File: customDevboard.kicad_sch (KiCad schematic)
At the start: 78 parts, among them J1 USB_C_Receptacle_USB2.0_14P, J10 GPIO29_ADC3, J11 GND, J12 GPIO0, J13 GPIO1, J14 GPIO2, J15 GPIO3, J16 GPIO4, J17 GPIO5, J18 GPIO6, J19 GPIO7, J2 RUN, J20 GPIO8, J21 GPIO9, J22 Conn_01x01, J23 Conn_01x01, J24 Conn_01x01, J25 Conn_01x01, J26 Conn_01x01, J27 Conn_01x01, J28 Conn_01x01, J29 Conn_01x01, J3 3V3, J30 Conn_01x01, J31 Conn_01x01, J32 Conn_01x01, J33 Conn_01x01, J34 Conn_01x01, J35 Conn_01x01, J36 Conn_01x01, J37 Conn_01x01, J38 Conn_01x01, J39 Conn_01x01, J4 VBUS, J40 Conn_01x01, J41 Conn_01x01, J42 SWCLK, J43 GND, J44 SWD, J5 GND, J6 GND, J7 GPIO26_ADC0, J8 GPIO27_ADC1, J9 GPIO28_ADC2, SW1 BOOT, U1 RP2040, U2 W25Q128JVP, U3 TLV75733PDRV, Y1 12 MHz

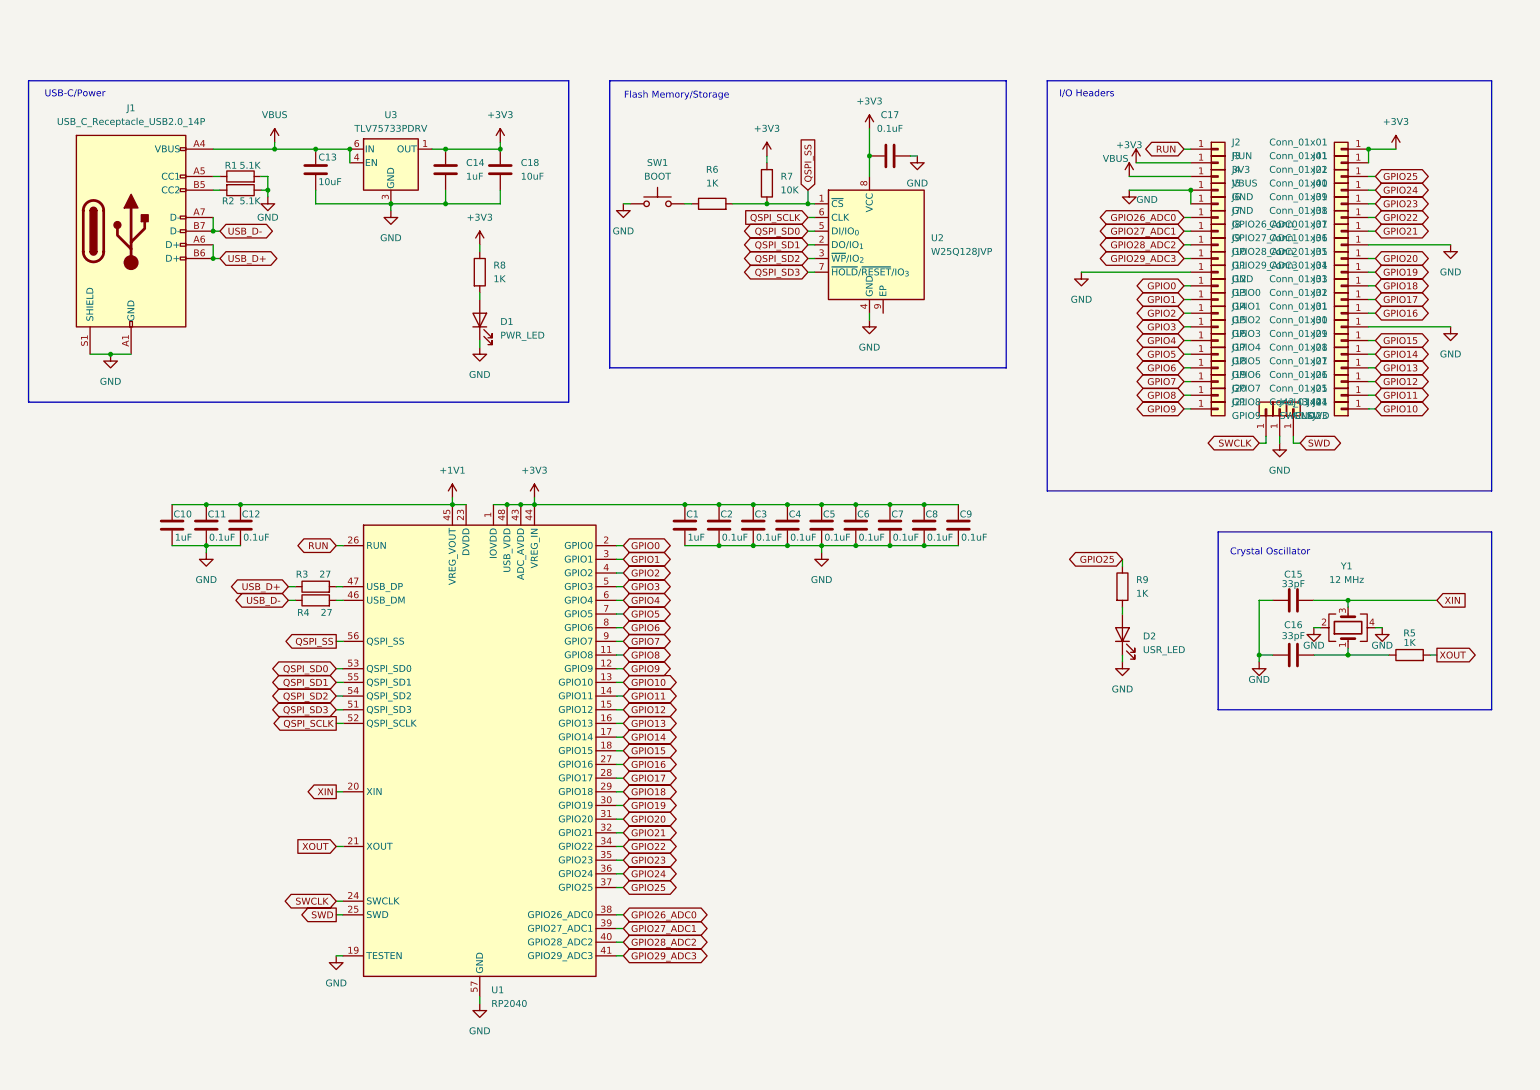
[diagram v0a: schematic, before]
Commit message: switch to stm32
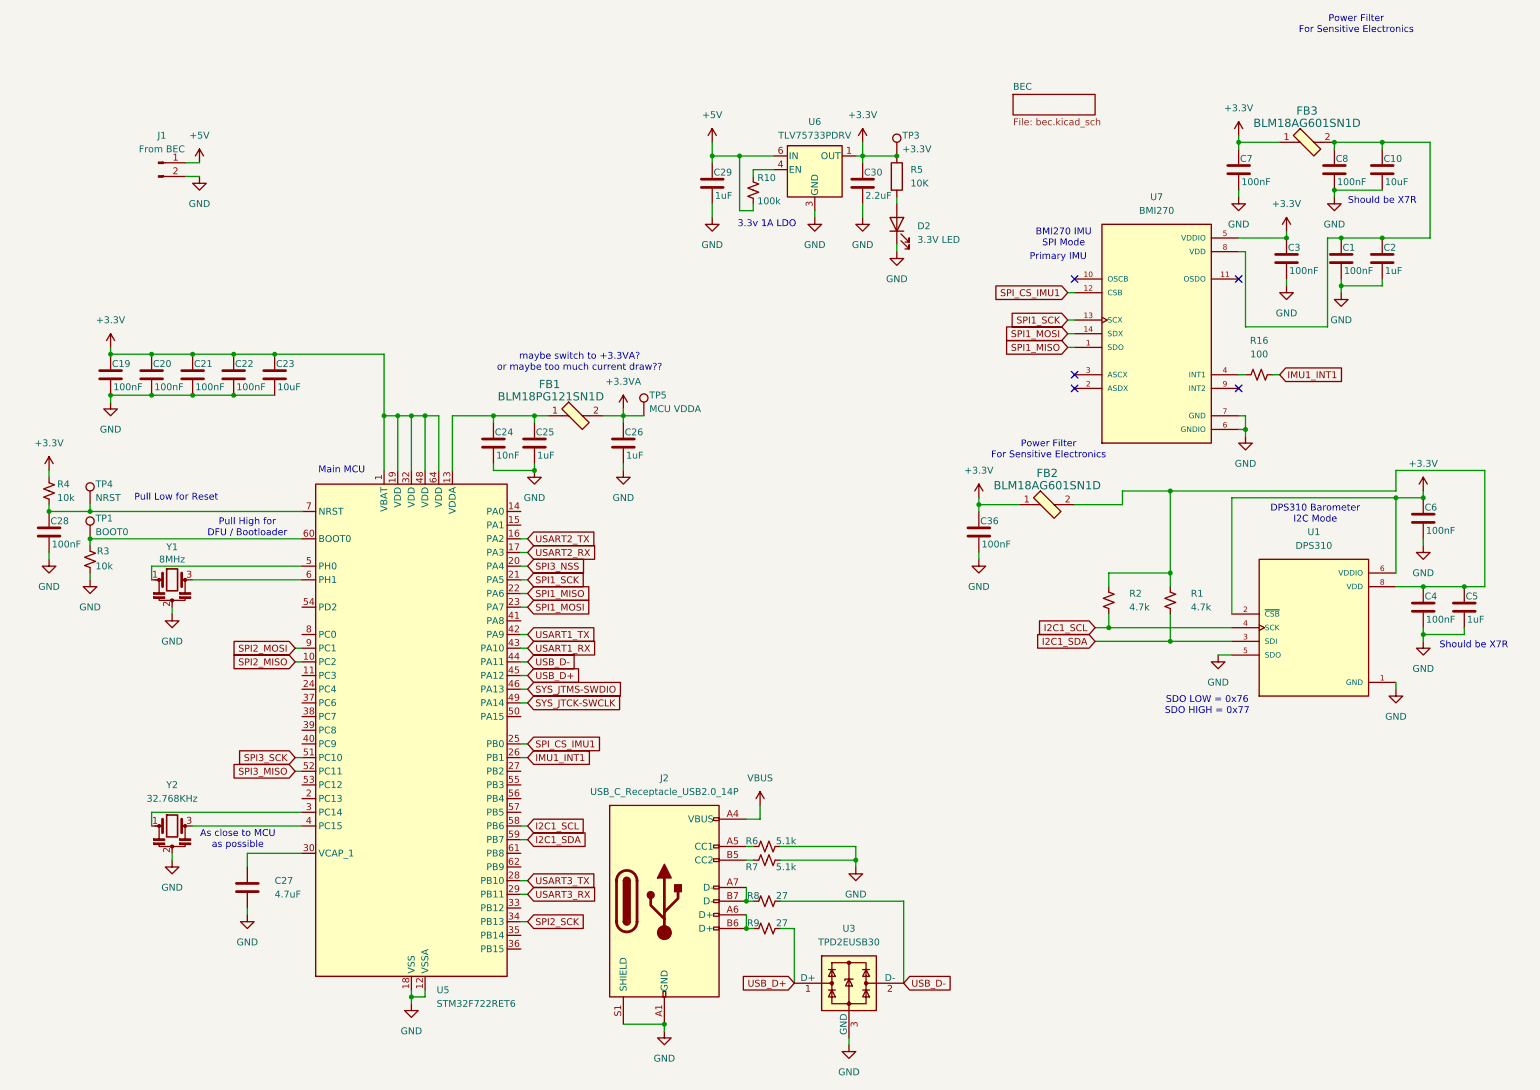
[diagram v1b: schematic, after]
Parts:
- removed C11, C12, C17, C9: 0.1uF, Capacitor_SMD:C_0402_1005Metric, symbol Device:C
- removed C13, C18: 10uF, Capacitor_SMD:C_0402_1005Metric, symbol Device:C
- removed C14: 1uF, Capacitor_SMD:C_0402_1005Metric, symbol Device:C
- removed C15, C16: 33pF, Capacitor_SMD:C_0402_1005Metric, symbol Device:C
- removed D1: PWR_LED, LED_SMD:LED_0402_1005Metric, symbol Device:LED
- removed J1: USB_C_Receptacle_USB2.0_14P, Connector_USB:USB_C_Receptacle_HRO_TYPE-C-31-M-12, symbol Connector:USB_C_Receptacle_USB2.0_14P
- removed J10: GPIO29_ADC3, Connector_Wire:SolderWirePad_1x01_SMD_1x2mm, symbol Connector_Generic:Conn_01x01
- removed J11, J43, J5, J6: GND, Connector_Wire:SolderWirePad_1x01_SMD_1x2mm, symbol Connector_Generic:Conn_01x01
- removed J12: GPIO0, Connector_Wire:SolderWirePad_1x01_SMD_1x2mm, symbol Connector_Generic:Conn_01x01
- removed J13: GPIO1, Connector_Wire:SolderWirePad_1x01_SMD_1x2mm, symbol Connector_Generic:Conn_01x01
- removed J14: GPIO2, Connector_Wire:SolderWirePad_1x01_SMD_1x2mm, symbol Connector_Generic:Conn_01x01
- removed J15: GPIO3, Connector_Wire:SolderWirePad_1x01_SMD_1x2mm, symbol Connector_Generic:Conn_01x01
- removed J16: GPIO4, Connector_Wire:SolderWirePad_1x01_SMD_1x2mm, symbol Connector_Generic:Conn_01x01
- removed J17: GPIO5, Connector_Wire:SolderWirePad_1x01_SMD_1x2mm, symbol Connector_Generic:Conn_01x01
- removed J18: GPIO6, Connector_Wire:SolderWirePad_1x01_SMD_1x2mm, symbol Connector_Generic:Conn_01x01
- removed J19: GPIO7, Connector_Wire:SolderWirePad_1x01_SMD_1x2mm, symbol Connector_Generic:Conn_01x01
- removed J2: RUN, Connector_Wire:SolderWirePad_1x01_SMD_1x2mm, symbol Connector_Generic:Conn_01x01
- removed J20: GPIO8, Connector_Wire:SolderWirePad_1x01_SMD_1x2mm, symbol Connector_Generic:Conn_01x01
- removed J21: GPIO9, Connector_Wire:SolderWirePad_1x01_SMD_1x2mm, symbol Connector_Generic:Conn_01x01
- removed J22, J23, J24, J25, J26, J27, J28, J29, J30, J31, J32, J33, J34, J35, J36, J37, J38, J39, J40, J41: Conn_01x01, Connector_Wire:SolderWirePad_1x01_SMD_1x2mm, symbol Connector_Generic:Conn_01x01
- removed J3: 3V3, Connector_Wire:SolderWirePad_1x01_SMD_1x2mm, symbol Connector_Generic:Conn_01x01
- removed J4: VBUS, Connector_Wire:SolderWirePad_1x01_SMD_1x2mm, symbol Connector_Generic:Conn_01x01
- removed J42: SWCLK, Connector_Wire:SolderWirePad_1x01_SMD_1x2mm, symbol Connector_Generic:Conn_01x01
- removed J44: SWD, Connector_Wire:SolderWirePad_1x01_SMD_1x2mm, symbol Connector_Generic:Conn_01x01
- removed J7: GPIO26_ADC0, Connector_Wire:SolderWirePad_1x01_SMD_1x2mm, symbol Connector_Generic:Conn_01x01
- removed J8: GPIO27_ADC1, Connector_Wire:SolderWirePad_1x01_SMD_1x2mm, symbol Connector_Generic:Conn_01x01
- removed J9: GPIO28_ADC2, Connector_Wire:SolderWirePad_1x01_SMD_1x2mm, symbol Connector_Generic:Conn_01x01
- removed R1, R2: 5.1K, Resistor_SMD:R_0402_1005Metric, symbol Device:R
- removed R3, R4: 27, Resistor_SMD:R_0402_1005Metric, symbol Device:R
- removed R6, R8, R9: 1K, Resistor_SMD:R_0402_1005Metric, symbol Device:R
- removed R7: 10K, Resistor_SMD:R_0402_1005Metric, symbol Device:R
- removed SW1: BOOT, Button_Switch_SMD:SW_Push_SPST_NO_Alps_SKRK, symbol Switch:SW_Push
- removed U1: RP2040, Package_DFN_QFN:QFN-56-1EP_7x7mm_P0.4mm_EP3.2x3.2mm, symbol MCU_RaspberryPi:RP2040
- removed U2: W25Q128JVP, Package_SON:WSON-8-1EP_6x5mm_P1.27mm_EP3.4x4.3mm, symbol Memory_Flash:W25Q128JVP
- removed U3: TLV75733PDRV, Package_SON:WSON-6-1EP_2x2mm_P0.65mm_EP1x1.6mm, symbol Regulator_Linear:TLV75733PDRV
- removed Y1: 12 MHz, Crystal:Crystal_SMD_3225-4Pin_3.2x2.5mm, symbol Device:Crystal_GND24
- added C19, C20, C21, C22: 100nF, Capacitor_SMD:C_0402_1005Metric_Pad0.74x0.62mm_HandSolder, symbol Device:C
- added C23: 10uF, Capacitor_SMD:C_0603_1608Metric_Pad1.08x0.95mm_HandSolder, symbol Device:C
- added C24: 10nF, Capacitor_SMD:C_0402_1005Metric_Pad0.74x0.62mm_HandSolder, symbol Device:C
- added C25, C26: 1uF, Capacitor_SMD:C_0402_1005Metric_Pad0.74x0.62mm_HandSolder, symbol Device:C
- added C27: 4.7uF, Capacitor_SMD:C_0603_1608Metric_Pad1.08x0.95mm_HandSolder, symbol Device:C
- added C28, C36: 100nF, Capacitor_SMD:C_0603_1608Metric_Pad1.08x0.95mm_HandSolder, symbol Device:C
- added C29: 1uF, Capacitor_SMD:C_0603_1608Metric_Pad1.08x0.95mm_HandSolder, symbol Device:C
- added C30: 2.2uF, Capacitor_SMD:C_0603_1608Metric_Pad1.08x0.95mm_HandSolder, symbol Device:C
- added FB1: BLM18PG121SN1D, digikey-footprints:0603, symbol dk_Ferrite-Beads-and-Chips:BLM18PG121SN1D
- added FB2, FB3: BLM18AG601SN1D, digikey-footprints:0603, symbol dk_Ferrite-Beads-and-Chips:BLM18AG601SN1D
- added J1: From BEC, Connector_PinHeader_2.54mm:PinHeader_1x02_P2.54mm_Vertical, symbol Connector:Conn_01x02_Pin
- added J2: USB_C_Receptacle_USB2.0_14P, Connector_USB:USB_C_Receptacle_HRO_TYPE-C-31-M-12, symbol Connector:USB_C_Receptacle_USB2.0_14P
- added R1, R2: 4.7k, Resistor_SMD:R_0603_1608Metric_Pad0.98x0.95mm_HandSolder, symbol Device:R_Small_US
- added R10: 100k, Resistor_SMD:R_0603_1608Metric_Pad0.98x0.95mm_HandSolder, symbol Device:R_Small_US
- added R16: 100, Resistor_SMD:R_0603_1608Metric_Pad0.98x0.95mm_HandSolder, symbol Device:R_Small_US
- added R3, R4: 10k, Resistor_SMD:R_0603_1608Metric_Pad0.98x0.95mm_HandSolder, symbol Device:R_Small_US
- added R6, R7: 5.1k, Resistor_SMD:R_0402_1005Metric_Pad0.72x0.64mm_HandSolder, symbol Device:R_Small_US
- added R8, R9: 27, Resistor_SMD:R_0402_1005Metric_Pad0.72x0.64mm_HandSolder, symbol Device:R_Small_US
- added TP1: BOOT0, TestPoint:TestPoint_Pad_1.0x1.0mm, symbol Connector:TestPoint
- added TP3: +3.3V, TestPoint:TestPoint_Pad_1.0x1.0mm, symbol Connector:TestPoint
- added TP4: NRST, TestPoint:TestPoint_Pad_1.0x1.0mm, symbol Connector:TestPoint
- added TP5: MCU VDDA, TestPoint:TestPoint_Pad_1.0x1.0mm, symbol Connector:TestPoint
- added U1: DPS310, DPS310:XDCR_DPS310, symbol DPS310:DPS310
- added U3: TPD2EUSB30, Package_TO_SOT_SMD:Texas_DRT-3, symbol Power_Protection:TPD2EUSB30
- added U5: STM32F722RET6, Package_QFP:LQFP-64_10x10mm_P0.5mm, symbol MCU_ST_STM32F7:STM32F722RETx
- added U6: TLV75733PDRV, Package_SON:WSON-6-1EP_2x2mm_P0.65mm_EP1x1.6mm, symbol Regulator_Linear:TLV75733PDRV
- added U7: BMI270, BMI270:XDCR_BMI270, symbol BMI270:BMI270
- added Y1: 8MHz, Crystal:Resonator_SMD_Murata_CSTxExxV-3Pin_3.0x1.1mm, symbol Device:Resonator
- added Y2: 32.768KHz, Crystal:Resonator_SMD_Murata_CSTxExxV-3Pin_3.0x1.1mm, symbol Device:Resonator
- C1: value 1uF -> 100nF; footprint Capacitor_SMD:C_0402_1005Metric -> Capacitor_SMD:C_0402_1005Metric_Pad0.74x0.62mm_HandSolder
- C10: value 1uF -> 10uF; footprint Capacitor_SMD:C_0402_1005Metric -> Capacitor_SMD:C_0603_1608Metric_Pad1.08x0.95mm_HandSolder
- C2, C5: value 0.1uF -> 1uF; footprint Capacitor_SMD:C_0402_1005Metric -> Capacitor_SMD:C_0402_1005Metric_Pad0.74x0.62mm_HandSolder
- C3, C4, C6: value 0.1uF -> 100nF; footprint Capacitor_SMD:C_0402_1005Metric -> Capacitor_SMD:C_0402_1005Metric_Pad0.74x0.62mm_HandSolder
- C7, C8: value 0.1uF -> 100nF; footprint Capacitor_SMD:C_0402_1005Metric -> Capacitor_SMD:C_0603_1608Metric_Pad1.08x0.95mm_HandSolder
- D2: value USR_LED -> 3.3V LED
- R5: value 1K -> 10K; footprint Resistor_SMD:R_0402_1005Metric -> Resistor_SMD:R_0603_1608Metric_Pad0.98x0.95mm_HandSolder
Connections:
- net XOUT is gone; now on an unnamed net: R5.2
- net GND: now also C19.2, C20.2, C21.2, C22.2, C23.2, C24.2, C25.2, C26.2, C27.2, C28.2, C29.2, C30.2, C36.2, J1.2 (Pin_2), J2.A1 (GND), J2.A12 (GND), J2.B1 (GND), J2.B12 (GND), J2.S1 (SHIELD), R3.2, R6.2, R7.1, U1.1 (GND), U1.5 (SDO), U1.7 (GND), U3.3 (GND), U5.12 (VSSA), U5.18 (VSS), U5.31 (VSS), U5.47 (VSS), U5.63 (VSS), U6.3 (GND), U6.7 (GND), U7.6 (GNDIO), U7.7 (GND), Y1.2, Y2.2
- net USB_D+: now also R9.1, U3.1 (D+), U5.45 (PA12)
- net USB_D-: now also R8.2, U3.2 (D-), U5.44 (PA11)
- net VBUS: now also J2.A4 (VBUS), J2.A9 (VBUS), J2.B4 (VBUS), J2.B9 (VBUS)
- net +3.3V: now reaches R5.1
- net +3.3V: now also C3.1, C6.1, C7.1, C19.1, C20.1, C21.1, C22.1, C23.1, C30.1, C36.1, FB2.1, FB3.1, R4.1, TP3.1, U1.2 (~{CSB}), U1.6 (VDDIO), U5.1 (VBAT), U5.19 (VDD), U5.32 (VDD), U5.48 (VDD), U5.64 (VDD), U6.1 (OUT), U7.5 (VDDIO)
- net +1V1: no longer names the net of C10.1
- net +1V1: now also C1.1, C2.1, C8.1, FB3.2, U7.8 (VDD)
- removed net +3V3: C1.1, C2.1, C3.1, C4.1, C5.1, C6.1, C7.1, C8.1
- new net: C24.1, C25.1, FB1.1, U5.13 (VDDA)
- new net: R10.1, U6.4 (EN)
- new net: C28.1, R4.2, TP4.1, U5.7 (NRST)
- new net: J2.A5 (CC1), R6.1
- new net: J2.A6 (D+), J2.B6 (D+), R9.2
- new net: J2.A7 (D-), J2.B7 (D-), R8.1
- new net: J2.B5 (CC2), R7.2
- new net: C4.1, C5.1, FB2.2, R1.1, R2.1, U1.8 (VDD)
- new net: C27.1, U5.30 (VCAP_1)
- new net: U5.3 (PC14), Y2.1
- new net: U5.4 (PC15), Y2.3
- new net: U5.5 (PH0), Y1.1
- new net: U5.6 (PH1), Y1.3
- new net: R16.1, U7.4 (INT1)
- new net: R3.1, TP1.1, U5.60 (BOOT0)
- new net +3.3VA: C26.1, FB1.2, TP5.1
- new net +5V: C29.1, J1.1 (Pin_1), R10.2, U6.6 (IN)
- new net I2C1_SCL: R2.2, U1.4 (SCK), U5.58 (PB6)
- new net I2C1_SDA: R1.2, U1.3 (SDI), U5.59 (PB7)
- new net IMU1_INT1: R16.2, U5.26 (PB1)
- new net SPI1_MISO: U5.22 (PA6), U7.1 (SDO)
- new net SPI1_MOSI: U5.23 (PA7), U7.14 (SDX)
- new net SPI1_SCK: U5.21 (PA5), U7.13 (SCX)
- new net SPI2_MISO: U5.10 (PC2)
- new net SPI2_MOSI: U5.9 (PC1)
- new net SPI2_SCK: U5.34 (PB13)
- new net SPI3_MISO: U5.52 (PC11)
- new net SPI3_NSS: U5.20 (PA4)
- new net SPI3_SCK: U5.51 (PC10)
- new net SPI_CS_IMU1: U5.25 (PB0), U7.12 (CSB)
- new net SYS_JTCK-SWCLK: U5.49 (PA14)
- new net SYS_JTMS-SWDIO: U5.46 (PA13)
- new net USART1_RX: U5.43 (PA10)
- new net USART1_TX: U5.42 (PA9)
- new net USART2_RX: U5.17 (PA3)
- new net USART2_TX: U5.16 (PA2)
- new net USART3_RX: U5.29 (PB11)
- new net USART3_TX: U5.28 (PB10)
- no-connect marks 0 -> 5
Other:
- added sheet BEC (bec.kicad_sch)
- note added: "3.3v 1A LDO"
- note added: "As close to MCU as possible"
- note added: "BMI270 IMU SPI Mode"
- note added: "DPS310 Barometer I2C Mode"
- note added: "Main MCU"
- note added: "Power Filter For Sensitive Electronics"
- note added: "Primary IMU"
- note added: "Pull High for DFU / Bootloader"
- note added: "Pull Low for Reset"
- note added: "SDO LOW = 0x76 SDO HIGH = 0x77"
- note added: "Should be X7R"
- note added: "maybe switch to +3.3VA? or maybe too much current draw??"
- note removed: "Crystal Oscillator"
- note removed: "Flash Memory/Storage"
- note removed: "I/O Headers"
- note removed: "USB-C/Power"

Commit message: prepare to move esc, gps, bec to other project
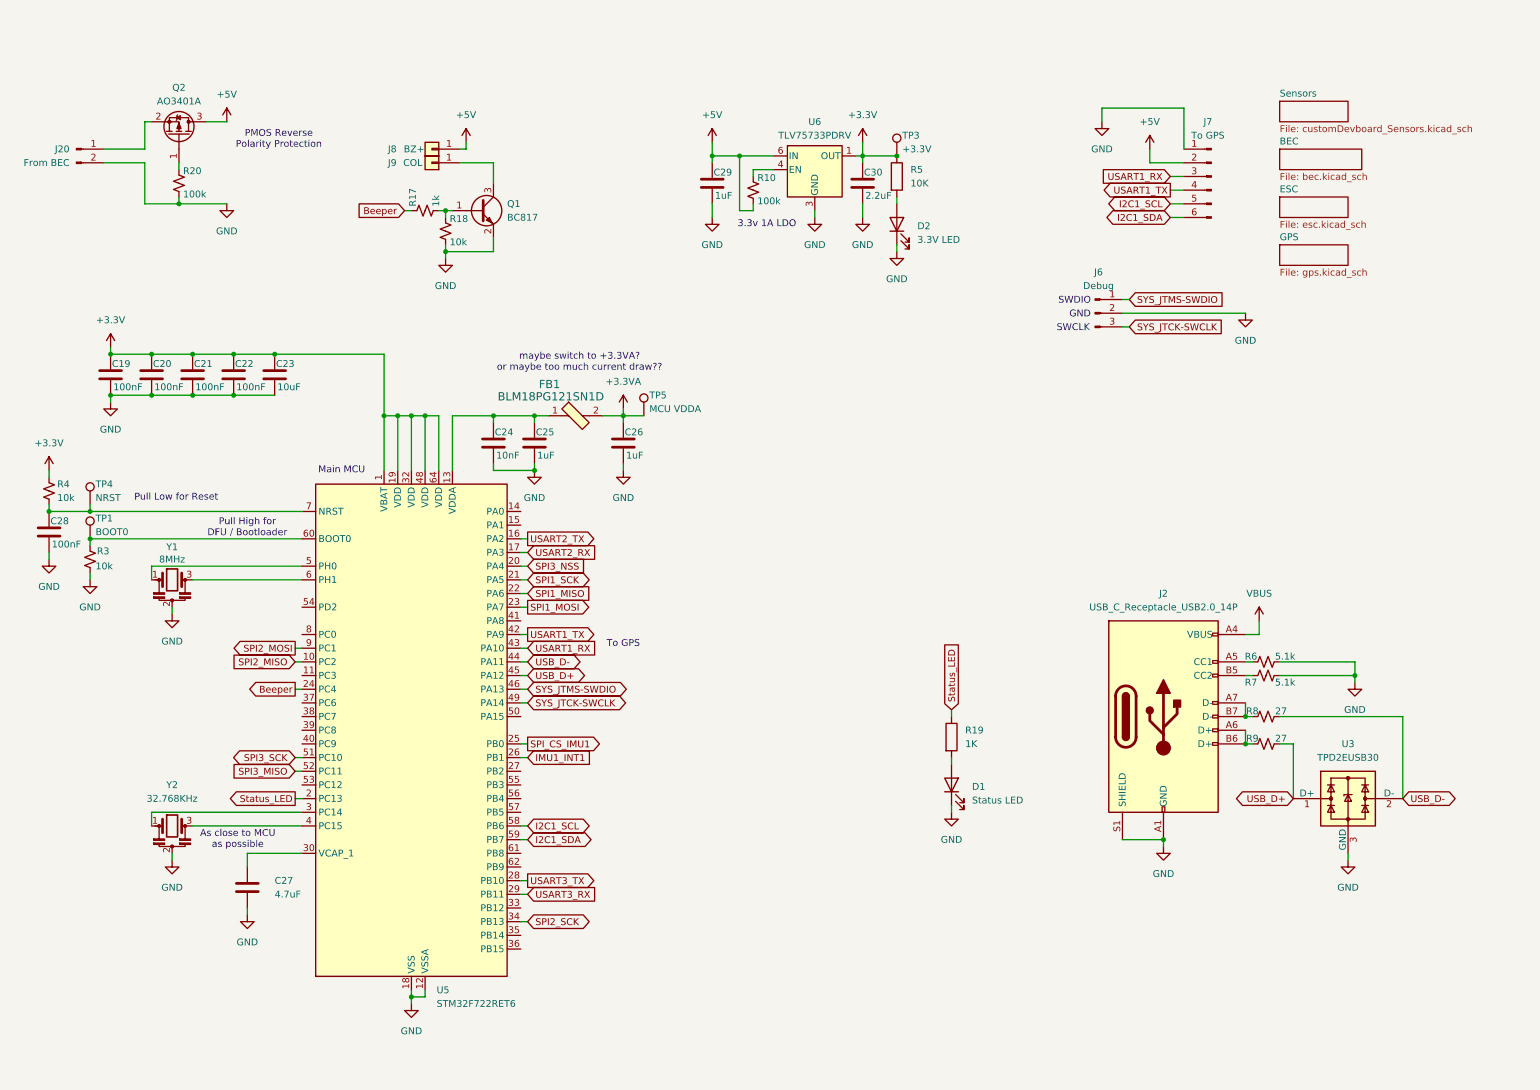
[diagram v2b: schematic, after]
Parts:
- removed C1, C3, C4, C6: 100nF, Capacitor_SMD:C_0402_1005Metric_Pad0.74x0.62mm_HandSolder, symbol Device:C
- removed C10: 10uF, Capacitor_SMD:C_0603_1608Metric_Pad1.08x0.95mm_HandSolder, symbol Device:C
- removed C2, C5: 1uF, Capacitor_SMD:C_0402_1005Metric_Pad0.74x0.62mm_HandSolder, symbol Device:C
- removed C36, C7, C8: 100nF, Capacitor_SMD:C_0603_1608Metric_Pad1.08x0.95mm_HandSolder, symbol Device:C
- removed FB2, FB3: BLM18AG601SN1D, digikey-footprints:0603, symbol dk_Ferrite-Beads-and-Chips:BLM18AG601SN1D
- removed J1: From BEC, Connector_PinHeader_2.54mm:PinHeader_1x02_P2.54mm_Vertical, symbol Connector:Conn_01x02_Pin
- removed R1, R2: 4.7k, Resistor_SMD:R_0603_1608Metric_Pad0.98x0.95mm_HandSolder, symbol Device:R_Small_US
- removed R16: 100, Resistor_SMD:R_0603_1608Metric_Pad0.98x0.95mm_HandSolder, symbol Device:R_Small_US
- removed U1: DPS310, DPS310:XDCR_DPS310, symbol DPS310:DPS310
- removed U7: BMI270, BMI270:XDCR_BMI270, symbol BMI270:BMI270
- added D1: Status LED, LED_SMD:LED_0603_1608Metric_Pad1.05x0.95mm_HandSolder, symbol Device:LED
- added J20: From BEC, Connector_Hirose:Hirose_DF13-02P-1.25DS_1x02_P1.25mm_Horizontal, symbol Connector:Conn_01x02_Pin
- added J6: Debug, Connector_PinHeader_2.54mm:PinHeader_1x03_P2.54mm_Vertical, symbol Connector:Conn_01x03_Pin
- added J7: To GPS, Connector_Hirose:Hirose_DF13-06P-1.25DS_1x06_P1.25mm_Horizontal, symbol Connector:Conn_01x06_Pin
- added J8: BZ+, Connector_Wire:SolderWirePad_1x01_SMD_1x2mm, symbol Connector_Generic:Conn_01x01
- added J9: COL, Connector_Wire:SolderWirePad_1x01_SMD_1x2mm, symbol Connector_Generic:Conn_01x01
- added Q1: BC817, digikey-footprints:SOT-23-3, symbol Transistor_BJT:BC817
- added Q2: AO3401A, Package_TO_SOT_SMD:SOT-23, symbol Transistor_FET:AO3401A
- added R17: 1k, Resistor_SMD:R_0603_1608Metric_Pad0.98x0.95mm_HandSolder, symbol Device:R_Small_US
- added R18: 10k, Resistor_SMD:R_0603_1608Metric_Pad0.98x0.95mm_HandSolder, symbol Device:R_Small_US
- added R19: 1K, Resistor_SMD:R_0603_1608Metric_Pad0.98x0.95mm_HandSolder, symbol Device:R
- added R20: 100k, Resistor_SMD:R_0603_1608Metric_Pad0.98x0.95mm_HandSolder, symbol Device:R_Small_US
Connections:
- net +5V: now also J7.2 (Pin_2), J8.1 (Pin_1), Q2.3 (D)
- net GND: now also D1.1 (K), J20.2 (Pin_2), J6.2 (Pin_2), J7.1 (Pin_1), Q1.2 (E), R18.2, R20.2
- net I2C1_SCL: now also J7.5 (Pin_5)
- net I2C1_SDA: now also J7.6 (Pin_6)
- net SYS_JTCK-SWCLK: now also J6.3 (Pin_3)
- net SYS_JTMS-SWDIO: now also J6.1 (Pin_1)
- net USART1_RX: now also J7.3 (Pin_3)
- net USART1_TX: now also J7.4 (Pin_4)
- net Status_LED: now reaches U5.2 (PC13)
- net Status_LED: now also R19.1
- net Beeper: now reaches U5.24 (PC4)
- net Beeper: now also R17.1
- new net: Q1.1 (B), R17.2, R18.1
- new net: J9.1 (Pin_1), Q1.3 (C)
- new net: J20.1 (Pin_1), Q2.2 (S)
- new net: Q2.1 (G), R20.1
- new net: D1.2 (A), R19.2
- no-connect marks 5 -> 0
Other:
- added sheet ESC (esc.kicad_sch)
- added sheet GPS (gps.kicad_sch)
- added sheet Sensors (customDevboard_Sensors.kicad_sch)
- note added: "GND"
- note added: "PMOS Reverse Polarity Protection"
- note added: "SWCLK"
- note added: "SWDIO"
- note added: "To GPS"
- note removed: "BMI270 IMU SPI Mode"
- note removed: "DPS310 Barometer I2C Mode"
- note removed: "Power Filter For Sensitive Electronics"
- note removed: "Primary IMU"
- note removed: "SDO LOW = 0x76 SDO HIGH = 0x77"
- note removed: "Should be X7R"
- moved on the sheet: J2, R6, R7, R8, R9, U3

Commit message: remove bec and gps
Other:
- removed sheet BEC
- removed sheet GPS
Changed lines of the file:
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@@
 	)
 	(sheet
-		(at 245.11 34.29)
+		(at 245.11 26.67)
 		(size 12.7 3.81)
 		(exclude_from_sim no)
@@
 		)
 		(property "Sheetname" "ESC"
-			(at 245.11 33.5784 0)
+			(at 245.11 25.9584 0)
 			(effects
 				(font
@@
 		)
 		(property "Sheetfile" "esc.kicad_sch"
-			(at 245.11 38.6846 0)
+			(at 245.11 31.0646 0)
 			(effects
 				(font
@@
 				)
 			)
-		)
-	)
-	(sheet
-		(at 245.11 25.4)
-		(size 15.24 3.81)
-		(exclude_from_sim no)
-		(in_bom yes)
-		(on_board yes)
-		(dnp no)
-		(fields_autoplaced yes)
-		(stroke
-			(width 0.1524)
-			(type solid)
-		)
-		(fill
-			(color 0 0 0 0.0000)
-		)
-		(property "Sheetname" "BEC"
-			(at 245.11 24.6884 0)
-			(effects
-				(font
-					(size 1.27 1.27)
-				)
-				(justify left bottom)
-			)
-		)
-		(property "Sheetfile" "bec.kicad_sch"
-			(at 245.11 29.7946 0)
-			(effects
-				(font
-					(size 1.27 1.27)
-				)
-				(justify left top)
-			)
-		)
-		(instances
-			(project "customDevboard"
-				(path "/87078d80-bd64-4f8e-8d0b-a79df4010aa3"
-					(page "2")
-				)
-			)
-		)
-	)
-	(sheet
-		(at 245.11 43.18)
-		(size 12.7 3.81)
-		(exclude_from_sim no)
-		(in_bom yes)
-		(on_board yes)
-		(dnp no)
-		(fields_autoplaced yes)
-		(stroke
-			(width 0.1524)
-			(type solid)
-		)
-		(fill
-			(color 0 0 0 0.0000)
-		)
-		(property "Sheetname" "GPS"
-			(at 245.11 42.4684 0)
-			(effects
-				(font
-					(size 1.27 1.27)
-				)
-				(justify left bottom)
-			)
-		)
-		(property "Sheetfile" "gps.kicad_sch"
-			(at 245.11 47.5746 0)
-			(effects
-				(font
-					(size 1.27 1.27)
-				)
-				(justify left top)
-			)
-		)
-		(instances
-			(project "customDevboard"
-				(path "/87078d80-bd64-4f8e-8d0b-a79df4010aa3"
-					(page "4")
-				)
-			)
